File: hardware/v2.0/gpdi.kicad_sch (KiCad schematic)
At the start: 20 parts, among them J2 GPDI_C_1.3, U1 ECP5U-25F-CABGA256, U5 TPD2EUSB30A, U6 PCA9306DC1

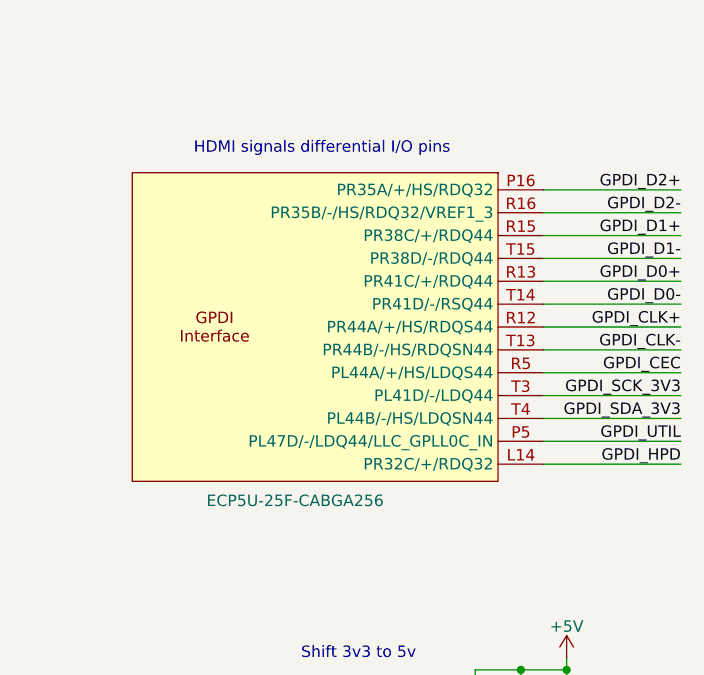
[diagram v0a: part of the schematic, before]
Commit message: ADC 6 diff lines
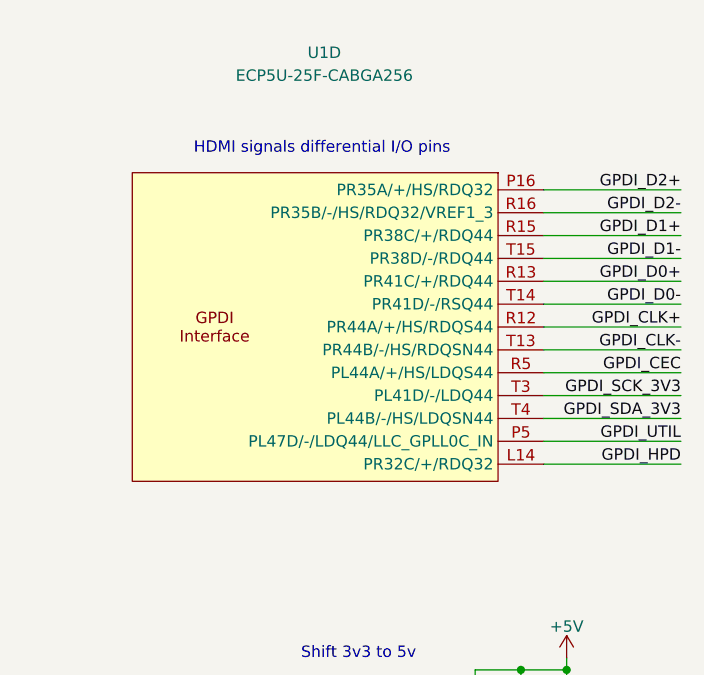
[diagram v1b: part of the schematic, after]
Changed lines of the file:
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@@
 		(dnp no)
 		(property "Reference" "U1"
-			(at 88.138 8.382 0)
+			(at 87.376 45.72 0)
 			(effects
 				(font
 					(size 1.27 1.27)
 				)
-				(hide yes)
 			)
 		)
 		(property "Value" "ECP5U-25F-CABGA256"
-			(at 93.98 95.504 0)
+			(at 87.376 48.26 0)
 			(effects
 				(font
 					(size 1.27 1.27)
 				)
-				(justify left)
 			)
 		)
@@
 					(reference "U1")
 					(unit 4)
+				)
+				(path "/f88da08e-cf42-4d03-a08f-3f602fe6658d/b5a9aa02-311b-4a9a-a7d4-646f15cdd9c2"
+					(reference "U1")
+					(unit 4)

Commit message: ADC CLKOUT±
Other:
- company: Chengyin Yao (cheyao), Vadym Vikulin -> Vadym Vikulin, Chengyin Yao (cheyao)
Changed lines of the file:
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@@
 	(title_block
 		(title "Icepi Zero")
-		(date "2026-01-05")
-		(rev "v2.0")
-		(company "Chengyin Yao (cheyao), Vadym Vikulin")
-		(comment 1 "https://github.com/cheyao/icepi-zero")
+		(date "2026-01-17")
+		(rev "v2.1")
+		(company "Vadym Vikulin, Chengyin Yao (cheyao)")
+		(comment 1 "https://github.com/vikulin/icepi-zero")
 		(comment 2 "License: Solderpad")
 		(comment 9 "OSHWA FR000026")
@@
 		(pin "P11"
 		)
+		(pin "N6"
+		)
 		(instances

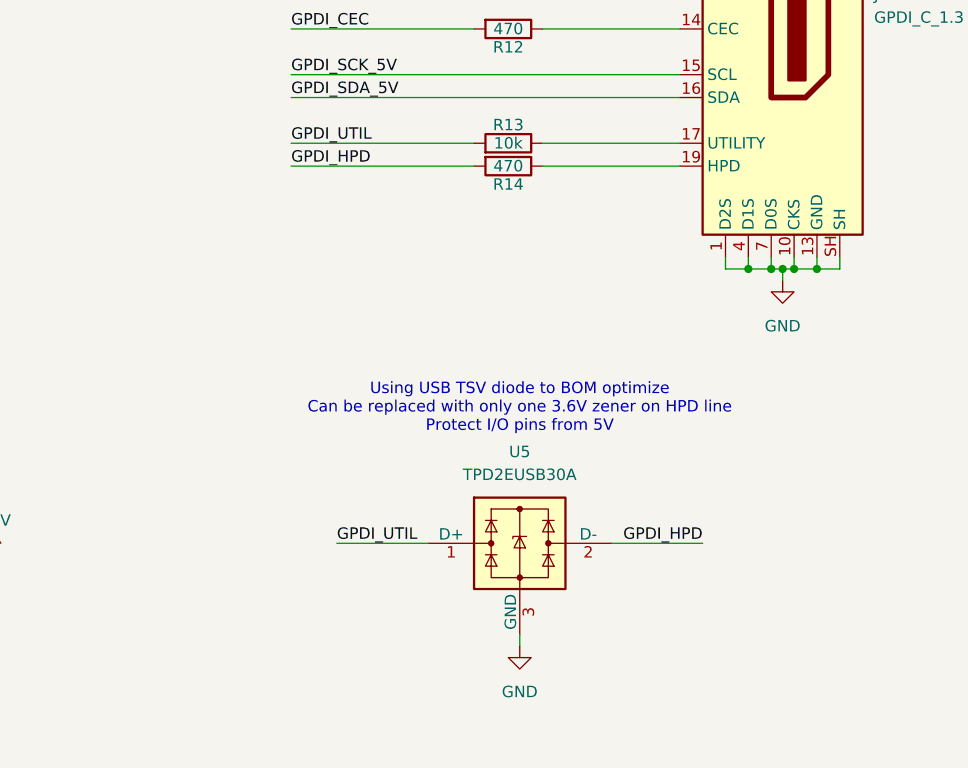
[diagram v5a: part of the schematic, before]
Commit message: HPD line protection
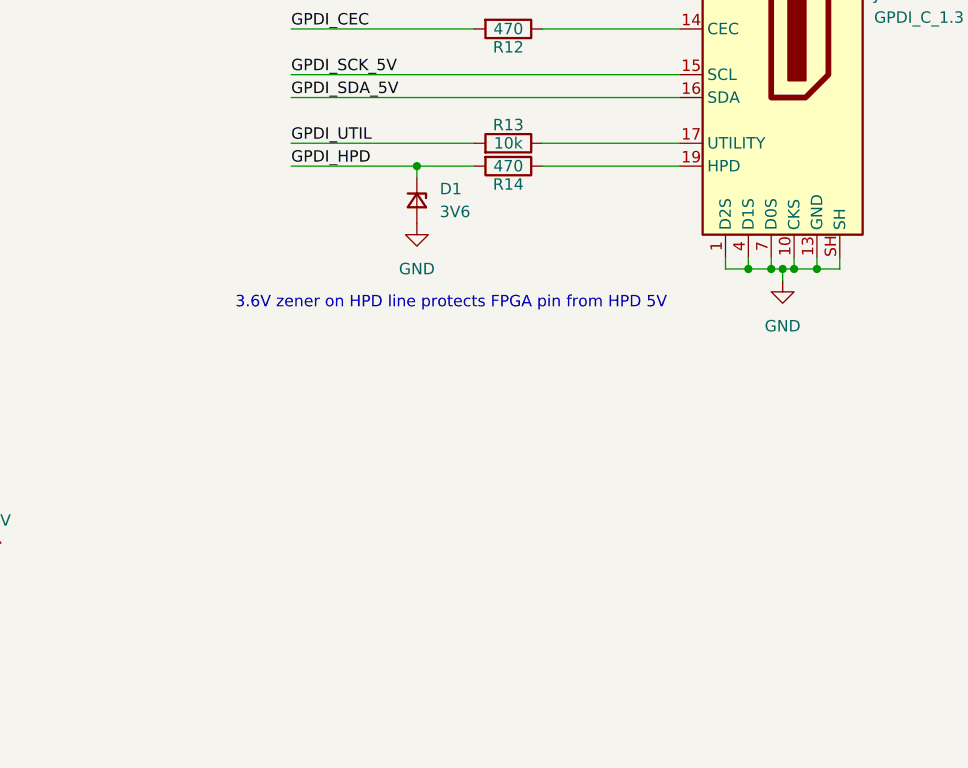
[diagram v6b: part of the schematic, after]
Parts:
- removed U5: TPD2EUSB30A, Package_TO_SOT_SMD:Texas_DRT-3, symbol Power_Protection:TPD2EUSB30A
- added D1: 3V6, Diode_SMD:D_SOD-323_HandSoldering, symbol Device:D_Zener_Small
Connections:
- net GND: now also D1.2 (A)
- net GPDI_HPD: now also D1.1 (K)
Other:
- note added: "3.6V zener on HPD line protects FPGA pin from HPD 5V"
- note removed: "Using USB TSV diode to BOM optimize Can be replaced with only one 3.6V zener on HPD line Protect I/O pins from 5V"
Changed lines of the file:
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@@
 		)
 	)
-	(text "Using USB TSV diode to BOM optimize\nCan be replaced with only one 3.6V zener on HPD line\nProtect I/O pins from 5V"
+	(text "3.6V zener on HPD line protects FPGA pin from HPD 5V"
 		(exclude_from_sim no)
-		(at 186.69 122.174 0)
+		(at 179.07 110.49 0)
 		(effects
 			(font
@@
 	)
 	(junction
+		(at 175.26 95.25)
+		(diameter 0)
+		(color 0 0 0 0)
+	)
+	(junction
 		(at 212.09 106.68)
 		(diameter 0)
@@
 	(wire
 		(pts
-			(xy 166.37 137.16) (xy 176.53 137.16)
-		)
-		(stroke
-			(width 0)
-			(type default)
-		)
-	)
-	(wire
-		(pts
 			(xy 215.9 107.95) (xy 215.9 106.68)
 		)
@@
 	(wire
 		(pts
+			(xy 175.26 96.52) (xy 175.26 95.25)
+		)
+		(stroke
+			(width 0)
+			(type default)
+		)
+	)
+	(wire
+		(pts
 			(xy 111.76 60.96) (xy 127 60.96)
 		)
@@
 	(wire
 		(pts
-			(xy 161.29 95.25) (xy 181.61 95.25)
+			(xy 161.29 95.25) (xy 175.26 95.25)
 		)
 		(stroke
@@
 	(wire
 		(pts
-			(xy 186.69 147.32) (xy 186.69 148.59)
-		)
-		(stroke
-			(width 0)
-			(type default)
-		)
-	)
-	(wire
-		(pts
 			(xy 111.76 66.04) (xy 127 66.04)
 		)
@@
 	(wire
 		(pts
-			(xy 196.85 137.16) (xy 207.01 137.16)
+			(xy 175.26 95.25) (xy 181.61 95.25)
 		)
 		(stroke
@@
 		)
 	)
-	(label "GPDI_UTIL"
-		(at 166.37 137.16 0)
-		(effects
-			(font
-				(size 1.27 1.27)
-			)
-			(justify left bottom)
-		)
-	)
 	(label "GPDI_CEC"
 		(at 161.29 80.01 0)
@@
 		)
 	)
-	(label "GPDI_HPD"
-		(at 207.01 137.16 180)
-		(effects
-			(font
-				(size 1.27 1.27)
-			)
-			(justify right bottom)
-		)
-	)
 	(label "GPDI_D0+"
 		(at 161.29 67.31 0)
@@
 	)
 	(symbol
+		(lib_id "Device:D_Zener_Small")
+		(at 175.26 99.06 270)
+		(unit 1)
+		(exclude_from_sim no)
+		(in_bom yes)
+		(on_board yes)
+		(dnp no)
+		(fields_autoplaced yes)
+		(property "Reference" "D1"
+			(at 177.8 97.7899 90)
+			(effects
+				(font
+					(size 1.27 1.27)
+				)
+				(justify left)
+			)
+		)
+		(property "Value" "3V6"
+			(at 177.8 100.3299 90)
+			(effects
+				(font
+					(size 1.27 1.27)
+				)
+				(justify left)
+			)
+		)
+		(property "Footprint" "Diode_SMD:D_SOD-323_HandSoldering"
+			(at 175.26 99.06 90)
+			(effects
+				(font
+					(size 1.27 1.27)
+				)
+				(hide yes)
+			)
+		)
+		(property "Datasheet" "~"
+			(at 175.26 99.06 90)
+			(effects
+				(font
+					(size 1.27 1.27)
+				)
+				(hide yes)
+			)
+		)
+		(property "Description" "Zener diode, small symbol"
+			(at 175.26 99.06 0)
+			(effects
+				(font
+					(size 1.27 1.27)
+				)
+				(hide yes)
+			)
+		)
+		(property "LCSC Part #" "C19077438"
+			(at 175.26 99.06 90)
+			(effects
+				(font
+					(size 1.27 1.27)
+				)
+				(hide yes)
+			)
+		)
+		(property "LCSC Link" "https://www.lcsc.com/product-detail/C19077438.html"
+			(at 175.26 99.06 90)
+			(effects
+				(font
+					(size 1.27 1.27)
+				)
+				(hide yes)
+			)
+		)
+		(property "Manufactuer Part Number" "C19077438"
+			(at 175.26 99.06 90)
+			(effects
+				(font
+					(size 1.27 1.27)
+				)
+				(hide yes)
+			)
+		)
+		(pin "2"
+		)
+		(pin "1"
+		)
+		(instances
+			(project ""
+				(path "/f88da08e-cf42-4d03-a08f-3f602fe6658d/efe0a411-ae63-4682-aa63-a9a30697cd67"
+					(reference "D1")
+					(unit 1)
+				)
+			)
+		)
+	)
+	(symbol
 		(lib_id "Device:C_Small")
 		(at 180.34 62.23 90)
@@
 	)
 	(symbol
-		(lib_id "Power_Protection:TPD2EUSB30A")
-		(at 186.69 137.16 0)
+		(lib_id "power:GND")
+		(at 175.26 101.6 0)
 		(unit 1)
 		(exclude_from_sim no)
@@
 		(dnp no)
 		(fields_autoplaced yes)
-		(property "Reference" "U5"
-			(at 186.69 127 0)
-			(effects
-				(font
-					(size 1.27 1.27)
-				)
-			)
-		)
-		(property "Value" "TPD2EUSB30A"
-			(at 186.69 129.54 0)
-			(effects
-				(font
-					(size 1.27 1.27)
-				)
-			)
-		)
-		(property "Footprint" "Package_TO_SOT_SMD:Texas_DRT-3"
-			(at 167.64 144.78 0)
+		(property "Reference" "#PWR0144"
+			(at 175.26 107.95 0)
 			(effects
 				(font
@@
 			)
 		)
-		(property "Datasheet" "http://www.ti.com/lit/ds/symlink/tpd2eusb30a.pdf"
-			(at 186.69 137.16 0)
-			(effects
-				(font
-					(size 1.27 1.27)
-				)
-				(hide yes)
-			)
-		)
-		(property "Description" "2-Channel ESD Protection for Super-Speed USB 3.0 Interface, DRT-3"
-			(at 186.69 137.16 0)
-			(effects
-				(font
-					(size 1.27 1.27)
-				)
-				(hide yes)
-			)
-		)
-		(property "LCSC Part #" "C3011197"
-			(at 186.69 137.16 0)
-			(effects
-				(font
-					(size 1.27 1.27)
-				)
-				(hide yes)
-			)
-		)
-		(property "LCSC Link" "https://lcsc.com/product-detail/ESD-and-Surge-Protection-TVS-ESD_TECH-PUBLIC-TPD2EUSB30ADRTR_C3011197.html"
-			(at 186.69 137.16 0)
+		(property "Value" "GND"
+			(at 175.26 106.68 0)
 			(effects
 				(font
 					(size 1.27 1.27)
 				)
-				(hide yes)
 			)
 		)
-		(property "Manufactuer Part Number" "TPD2EUSB30ADRTR"
-			(at 186.69 137.16 0)
+		(property "Footprint" ""
+			(at 175.26 101.6 0)
 			(effects
 				(font
@@
 			)
 		)
-		(property "Note" ""
-			(at 186.69 137.16 0)
+		(property "Datasheet" ""
+			(at 175.26 101.6 0)
 			(effects
 				(font
@@
 			)
 		)
-		(property "Notes" ""
-			(at 186.69 137.16 0)
+		(property "Description" "Power symbol creates a global label with name \"GND\" , ground"
+			(at 175.26 101.6 0)
 			(effects
 				(font
@@
 			)
 		)
-		(pin "2"
-		)
-		(pin "3"
-		)
 		(pin "1"
 		)
@@
 			(project "icepi-zero"
 				(path "/f88da08e-cf42-4d03-a08f-3f602fe6658d/efe0a411-ae63-4682-aa63-a9a30697cd67"
-					(reference "U5")
+					(reference "#PWR0144")
 					(unit 1)
 				)
@@
 					(unit 1)
 				)
-			)
-		)
-	)
-	(symbol
-		(lib_id "power:GND")
-		(at 186.69 148.59 0)
-		(unit 1)
-		(exclude_from_sim no)
-		(in_bom yes)
-		(on_board yes)
-		(dnp no)
-		(fields_autoplaced yes)
-		(property "Reference" "#PWR059"
-			(at 186.69 154.94 0)
-			(effects
-				(font
-					(size 1.27 1.27)
-				)
-				(hide yes)
-			)
-		)
-		(property "Value" "GND"
-			(at 186.69 153.67 0)
-			(effects
-				(font
-					(size 1.27 1.27)
-				)
-			)
-		)
-		(property "Footprint" ""
-			(at 186.69 148.59 0)
-			(effects
-				(font
-					(size 1.27 1.27)
-				)
-				(hide yes)
-			)
-		)
-		(property "Datasheet" ""
-			(at 186.69 148.59 0)
-			(effects
-				(font
-					(size 1.27 1.27)
-				)
-				(hide yes)
-			)
-		)
-		(property "Description" "Power symbol creates a global label with name \"GND\" , ground"
-			(at 186.69 148.59 0)
-			(effects
-				(font
-					(size 1.27 1.27)
-				)
-				(hide yes)
-			)
-		)
-		(pin "1"
-		)
-		(instances
-			(project "icepi-zero"
-				(path "/f88da08e-cf42-4d03-a08f-3f602fe6658d/efe0a411-ae63-4682-aa63-a9a30697cd67"
-					(reference "#PWR059")
-					(unit 1)
-				)

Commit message: Pads clearance fix
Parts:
- U6: footprint Package_SO:VSSOP-8_2.3x2mm_P0.5mm -> VSSOP-8_2.3x2mm_P0.5mm-exp-mask:VSSOP-8_2.3x2mm_P0.5mm
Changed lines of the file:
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@@
 			)
 		)
-		(property "Footprint" "Package_SO:VSSOP-8_2.3x2mm_P0.5mm"
+		(property "Footprint" "VSSOP-8_2.3x2mm_P0.5mm-exp-mask:VSSOP-8_2.3x2mm_P0.5mm"
 			(at 90.17 153.67 0)
 			(effects
